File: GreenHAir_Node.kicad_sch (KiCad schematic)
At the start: 0 parts

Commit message: worked on schematic
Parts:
- added FID101, FID102: Fiducial, symbol Mechanical:Fiducial
- added H101, H102, H103, H104: MountingHole_Pad, symbol Mechanical:MountingHole_Pad
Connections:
- new net GND: H101.1, H102.1, H103.1, H104.1
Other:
- added sheet Microcontroller (mcu.kicad_sch)
- added sheet Power Supply (psu.kicad_sch)
- added sheet Sensor (sensor.kicad_sch)
- company: (none) -> Perillion Labs

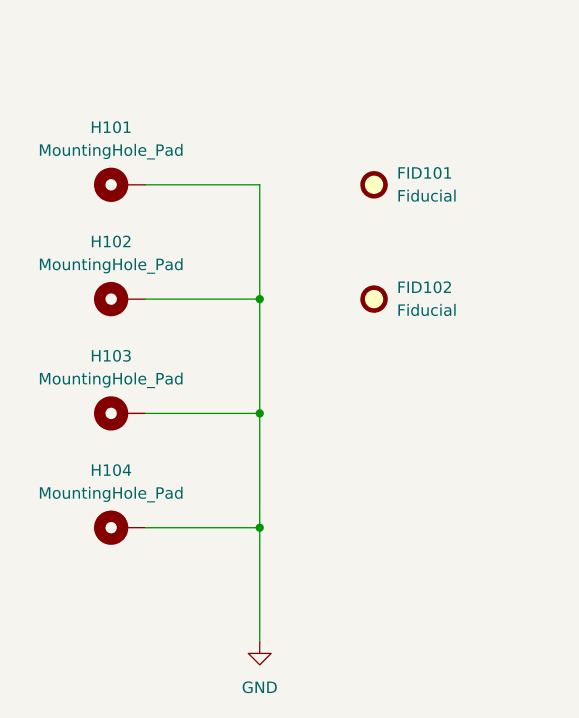
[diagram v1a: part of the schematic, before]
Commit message: Update Schematics - Add footprint to symbols.
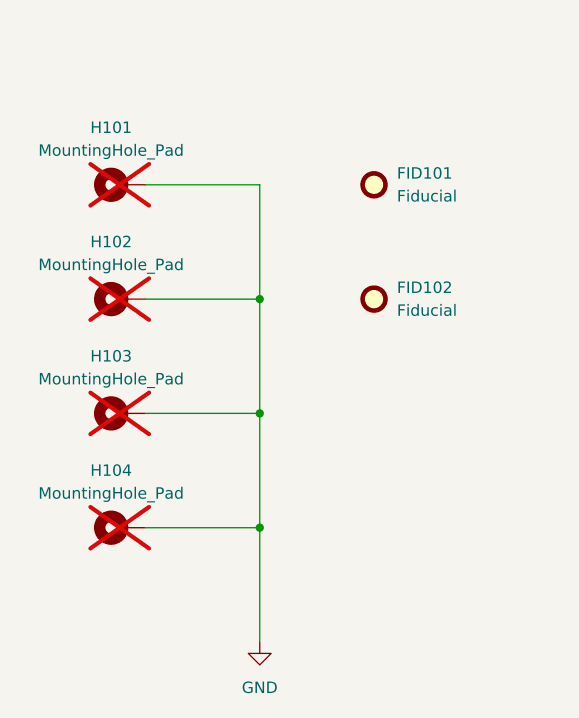
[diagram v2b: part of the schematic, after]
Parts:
- FID101, FID102: footprint (none) -> Fiducial:Fiducial_0.75mm_Mask1.5mm
- H101, H102, H103, H104: footprint (none) -> MountingHole:MountingHole_2.7mm_M2.5_ISO14580_Pad_TopBottom; now not fitted
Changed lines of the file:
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@@
-	(wire
-		(pts
-			(xy 50.8 177.8) (xy 50.8 165.1)
-		)
-		(stroke
-			(width 0)
-			(type default)
-		)
-	)
 	(wire
 		(pts
@@
 		(pts
 			(xy 38.1 152.4) (xy 50.8 152.4)
+		)
+		(stroke
+			(width 0)
+			(type default)
+		)
+	)
+	(wire
+		(pts
+			(xy 50.8 165.1) (xy 50.8 177.8)
 		)
 		(stroke
@@
 			)
 		)
-		(property "Footprint" ""
+		(property "Footprint" "Fiducial:Fiducial_0.75mm_Mask1.5mm"
 			(at 63.5 127 0)
 			(effects
@@
 		(in_bom no)
 		(on_board yes)
-		(dnp no)
+		(dnp yes)
 		(fields_autoplaced yes)
 		(property "Reference" "H101"
@@
 			)
 		)
-		(property "Footprint" ""
+		(property "Footprint" "MountingHole:MountingHole_2.7mm_M2.5_ISO14580_Pad_TopBottom"
 			(at 35.56 127 0)
 			(effects
@@
 			)
 		)
-		(property "Footprint" ""
+		(property "Footprint" "Fiducial:Fiducial_0.75mm_Mask1.5mm"
 			(at 63.5 139.7 0)
 			(effects
@@
 		(in_bom no)
 		(on_board yes)
-		(dnp no)
+		(dnp yes)
 		(fields_autoplaced yes)
 		(property "Reference" "H102"
@@
 			)
 		)
-		(property "Footprint" ""
+		(property "Footprint" "MountingHole:MountingHole_2.7mm_M2.5_ISO14580_Pad_TopBottom"
 			(at 35.56 139.7 0)
 			(effects
@@
 		(in_bom no)
 		(on_board yes)
-		(dnp no)
+		(dnp yes)
 		(fields_autoplaced yes)
 		(property "Reference" "H103"
@@
 			)
 		)
-		(property "Footprint" ""
+		(property "Footprint" "MountingHole:MountingHole_2.7mm_M2.5_ISO14580_Pad_TopBottom"
 			(at 35.56 152.4 0)
 			(effects
@@
 		(in_bom no)
 		(on_board yes)
-		(dnp no)
+		(dnp yes)
 		(fields_autoplaced yes)
 		(property "Reference" "H104"
@@
 			)
 		)
-		(property "Footprint" ""
+		(property "Footprint" "MountingHole:MountingHole_2.7mm_M2.5_ISO14580_Pad_TopBottom"
 			(at 35.56 165.1 0)
 			(effects
